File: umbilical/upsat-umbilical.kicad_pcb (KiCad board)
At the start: 2 copper layers, 21 x 16.5 mm, 4 parts, among them P1 CONN_5X2, P2 CONN_5X2

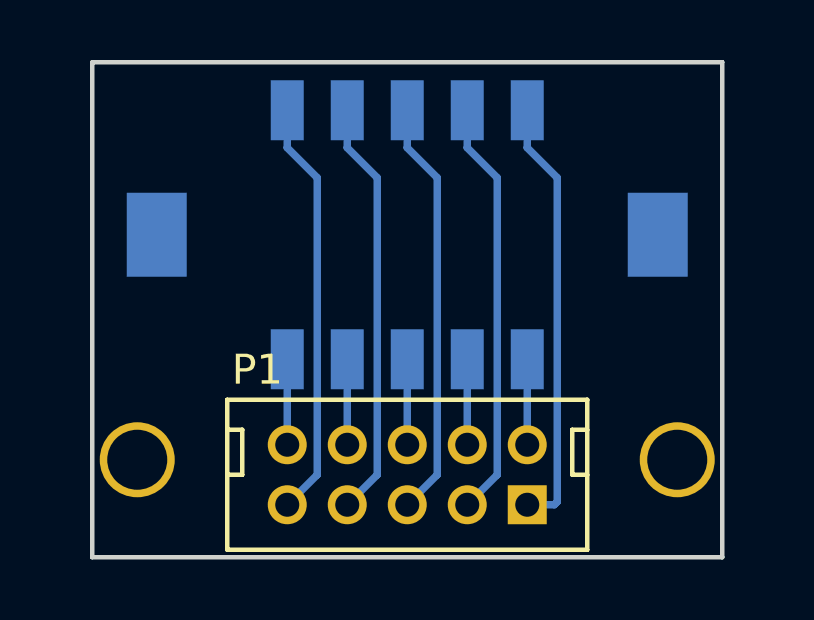
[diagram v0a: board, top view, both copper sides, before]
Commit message: Add umbilical and test pod.
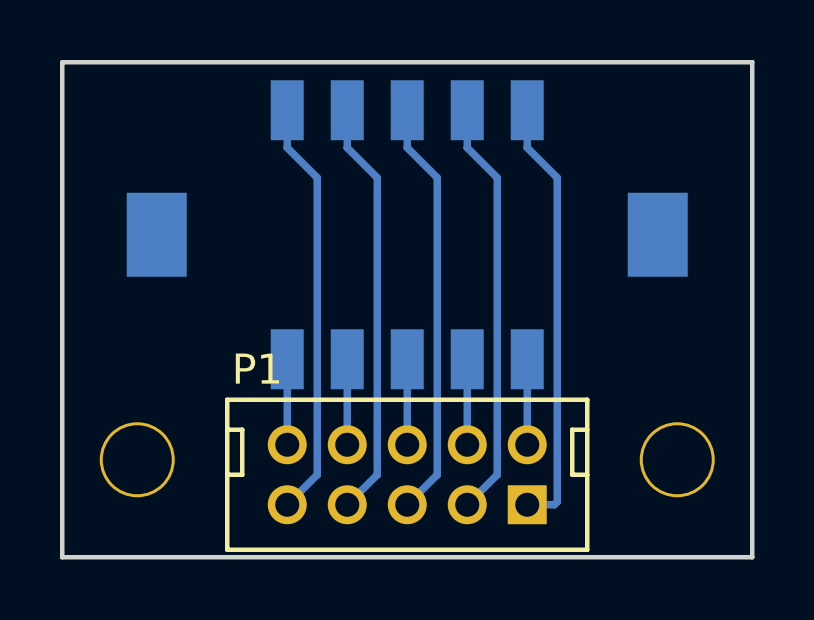
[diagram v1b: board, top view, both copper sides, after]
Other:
- board size 21 x 16.5 mm -> 23 x 16.5 mm
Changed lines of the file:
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@@
-(kicad_pcb (version 4) (host pcbnew 4.0.1-2.fc23-product)
+(kicad_pcb (version 4) (host pcbnew no-vcs-found-product)
   (general
-    (links 0)
-    (no_connects 10)
-    (area 137.924999 107.674999 159.075001 124.325001)
+    (links 10)
+    (no_connects 0)
+    (area 135.201191 107.674999 161.79881 126.0925)
     (thickness 1.6)
-    (drawings 6)
+    (drawings 4)
     (tracks 26)
     (zones 0)
@@
     (mod_text_size 1 1)
     (mod_text_width 0.15)
-    (pad_size 1.524 1.524)
-    (pad_drill 0.762)
+    (pad_size 2.5 2.5)
+    (pad_drill 2.3)
     (pad_to_mask_clearance 0.2)
     (aux_axis_origin 0 0)
     (visible_elements FFFFFF7F)
     (pcbplotparams
-      (layerselection 0x00030_80000001)
+      (layerselection 0x01000_fffffffe)
       (usegerberextensions false)
-      (excludeedgelayer true)
+      (excludeedgelayer false)
       (linewidth 0.100000)
       (plotframeref false)
@@
       (hpglpenspeed 20)
       (hpglpendiameter 15)
-      (hpglpenoverlay 2)
       (psnegative false)
       (psa4output false)
@@
       (padsonsilk false)
       (subtractmaskfromsilk false)
-      (outputformat 1)
+      (outputformat 5)
       (mirror false)
-      (drillshape 1)
+      (drillshape 2)
       (scaleselection 1)
-      (outputdirectory ""))
+      (outputdirectory gerber))
   )
   (net 0 "")
@@
       (effects (font (size 1 1) (thickness 0.15)))
     )
-    (pad 1 thru_hole circle (at 0 0) (size 2.5 2.5) (drill 2) (layers *.Cu *.Mask F.SilkS))
+    (pad 1 thru_hole circle (at 0 0) (size 2.5 2.5) (drill 2.3) (layers *.Cu *.Mask F.SilkS))
   )
   (module holes:2mm-hole (layer F.Cu)
@@
       (effects (font (size 1 1) (thickness 0.15)))
     )
-    (pad 1 thru_hole circle (at 0 0) (size 2.5 2.5) (drill 2) (layers *.Cu *.Mask F.SilkS))
-  )
-  (dimension 16.5 (width 0.3) (layer Dwgs.User)
-    (gr_text "16.500 mm" (at 162.6 116 90) (layer Dwgs.User)
-      (effects (font (size 1.5 1.5) (thickness 0.3)))
-    )
-    (feature1 (pts (xy 159 107.75) (xy 163.95 107.75)))
-    (feature2 (pts (xy 159 124.25) (xy 163.95 124.25)))
-    (crossbar (pts (xy 161.25 124.25) (xy 161.25 107.75)))
-    (arrow1a (pts (xy 161.25 107.75) (xy 161.836421 108.876504)))
-    (arrow1b (pts (xy 161.25 107.75) (xy 160.663579 108.876504)))
-    (arrow2a (pts (xy 161.25 124.25) (xy 161.836421 123.123496)))
-    (arrow2b (pts (xy 161.25 124.25) (xy 160.663579 123.123496)))
-  )
-  (dimension 21 (width 0.3) (layer Dwgs.User)
-    (gr_text "21.000 mm" (at 148.5 103.4) (layer Dwgs.User)
-      (effects (font (size 1.5 1.5) (thickness 0.3)))
-    )
-    (feature1 (pts (xy 159 107.75) (xy 159 102.05)))
-    (feature2 (pts (xy 138 107.75) (xy 138 102.05)))
-    (crossbar (pts (xy 138 104.75) (xy 159 104.75)))
-    (arrow1a (pts (xy 159 104.75) (xy 157.873496 105.336421)))
-    (arrow1b (pts (xy 159 104.75) (xy 157.873496 104.163579)))
-    (arrow2a (pts (xy 138 104.75) (xy 139.126504 105.336421)))
-    (arrow2b (pts (xy 138 104.75) (xy 139.126504 104.163579)))
-  )
-  (gr_line (start 138 124.25) (end 159 124.25) (layer Edge.Cuts) (width 0.15))
-  (gr_line (start 138 107.75) (end 138 124.25) (layer Edge.Cuts) (width 0.15))
-  (gr_line (start 159 107.75) (end 138 107.75) (layer Edge.Cuts) (width 0.15))
-  (gr_line (start 159 124.25) (end 159 107.75) (layer Edge.Cuts) (width 0.15))
+    (pad 1 thru_hole circle (at 0 0) (size 2.5 2.5) (drill 2.3) (layers *.Cu *.Mask F.SilkS))
+  )
+  (gr_line (start 137 124.25) (end 160 124.25) (layer Edge.Cuts) (width 0.15))
+  (gr_line (start 137 107.75) (end 137 124.25) (layer Edge.Cuts) (width 0.15))
+  (gr_line (start 160 107.75) (end 137 107.75) (layer Edge.Cuts) (width 0.15))
+  (gr_line (start 160 124.25) (end 160 107.75) (layer Edge.Cuts) (width 0.15))
   (segment (start 146.5 122.5) (end 147.5 121.5) (width 0.25) (layer B.Cu) (net 1))
   (segment (start 147.5 121.5) (end 147.5 111.6) (width 0.25) (layer B.Cu) (net 1))
